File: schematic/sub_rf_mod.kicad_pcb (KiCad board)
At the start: 2 copper layers, 69.1 x 50 mm, 39 parts, among them J4B1 Conn_01x08

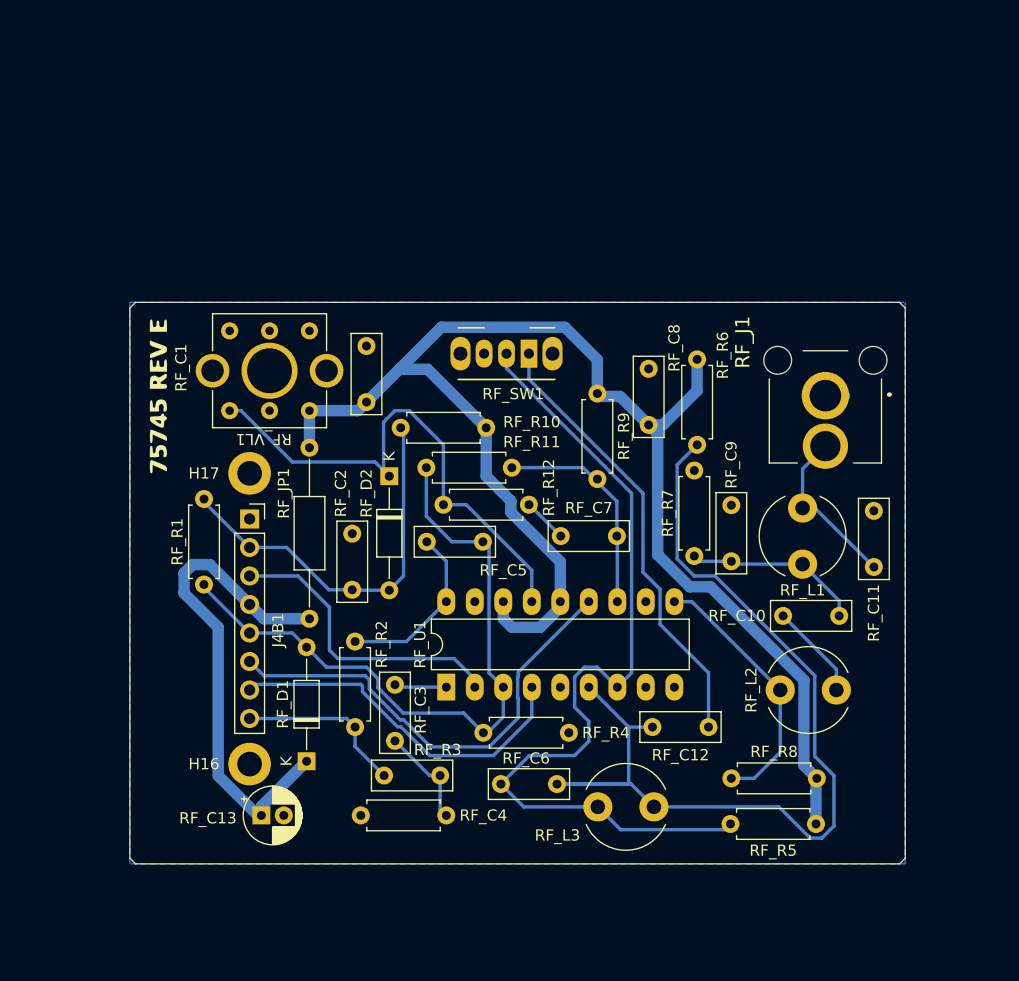
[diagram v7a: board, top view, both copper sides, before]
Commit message: adjusting RF layout, seems to have issues with the previous layout with noise
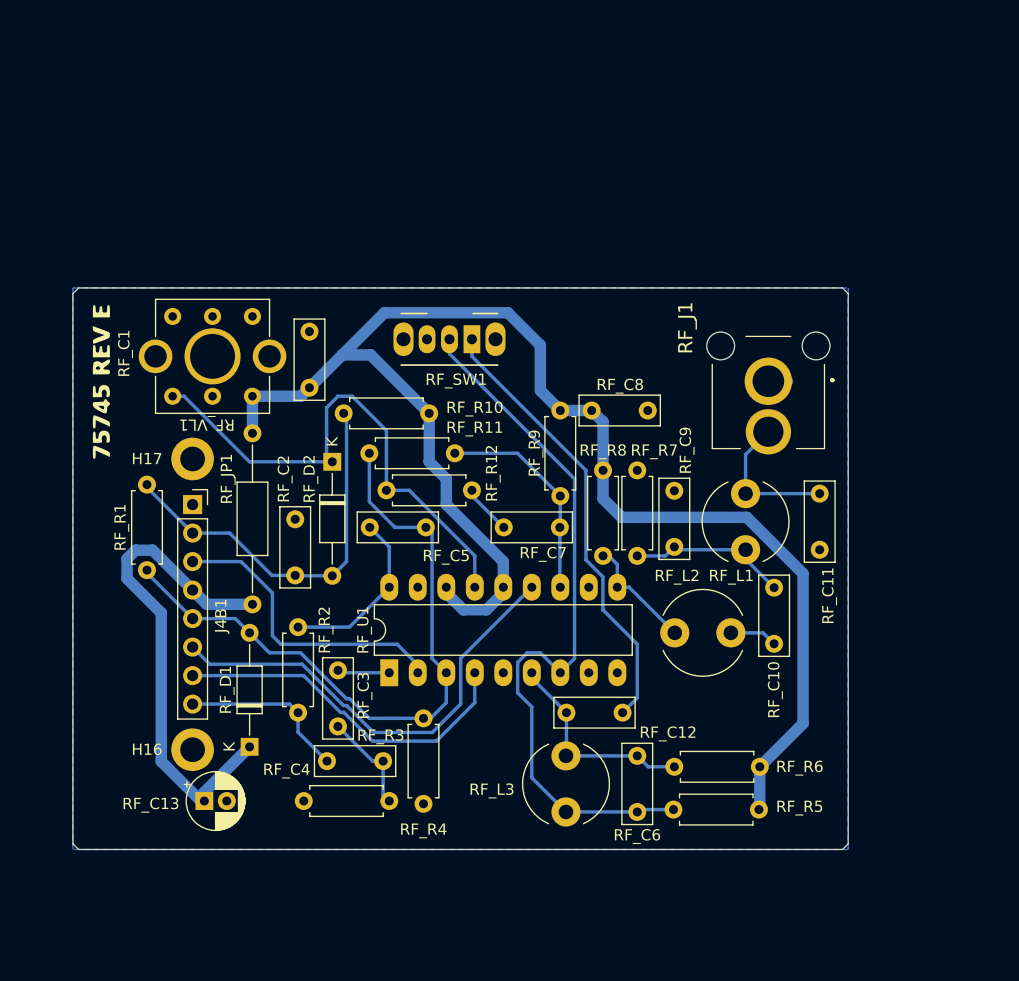
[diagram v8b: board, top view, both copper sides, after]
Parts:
- RF_R5, RF_R6: value 270R -> 240R
- moved RF_R6 28.8 mm to (158.8, 112.8), turned to 0 degrees
- moved RF_R8 22.9 mm to (152.4, 94.0), turned to 90 degrees
- moved RF_R4 14.4 mm to (136.4, 116.1), turned to 90 degrees
- moved RF_C6 12.4 mm to (155.4, 116.8), turned to 90 degrees
- moved RF_L2 10.7 mm to (158.8, 100.8)
- moved RF_C11 8.13 mm to (171.7, 88.4), turned to -90 degrees
- moved RF_C12 7.77 mm to (154.1, 107.9)
- moved RF_C3 5.24 mm to (128.8, 104.2)
- moved RF_C8 5.24 mm to (151.4, 81.0), turned to 0 degrees
- moved RF_U1 5.24 mm to (133.3, 104.4)
- moved RF_C1 5.24 mm to (126.2, 79.0)
- moved RF_C4 5.24 mm to (132.8, 112.3)
- moved RF_C5 5.24 mm to (131.6, 91.4)
- moved RF_C9 5.24 mm to (158.8, 93.2)
- moved RF_L1 5.24 mm to (165.1, 93.4)
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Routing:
- net (no net): track 755.5 -> 651.3 mm
